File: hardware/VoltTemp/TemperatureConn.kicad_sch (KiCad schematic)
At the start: 3 parts, among them J15 Conn_01x07, J6 Conn_01x04

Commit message: schematic mostly done
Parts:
- removed J15: Conn_01x07, symbol Connector_Generic:Conn_01x07
- added J8: Conn_01x06, VoltTemp:1053131106, symbol Connector_Generic:Conn_01x06
- added J9: Conn_01x03, VoltTemp:1053131103, symbol Connector_Generic:Conn_01x03
- J6: footprint (none) -> VoltTemp:1053132104; P/N (none) -> 1053132104
- R24: footprint Resistor_SMD:R_0805_2012Metric -> Resistor_SMD:R_0603_1608Metric_Pad0.98x0.95mm_HandSolder; P/N SMD_0805 -> (none)
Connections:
- net GNDA: now also J8.6 (Pin_6), J9.3 (Pin_3)
- net VDDA: now also J8.1 (Pin_1), J9.1 (Pin_1)
- net rawTemperature0: now also J6.2 (Pin_2), R24.1
- net rawTemperature1: now also J8.4 (Pin_4); no longer J6.2 (Pin_2), R24.1
- net rawTemperature2: now also J8.3 (Pin_3)
- net rawTemperature3: now also J8.2 (Pin_2)
- net rawTemperature4: now also J9.2 (Pin_2)
- net rawTemperature1_Pre renamed rawTemperature0_Pre
- net rawTemperature0_Pre: now also J8.5 (Pin_5)
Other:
- note added: "Extra Temperature Breakout"
- note added: "Thermistor Collector Connector"

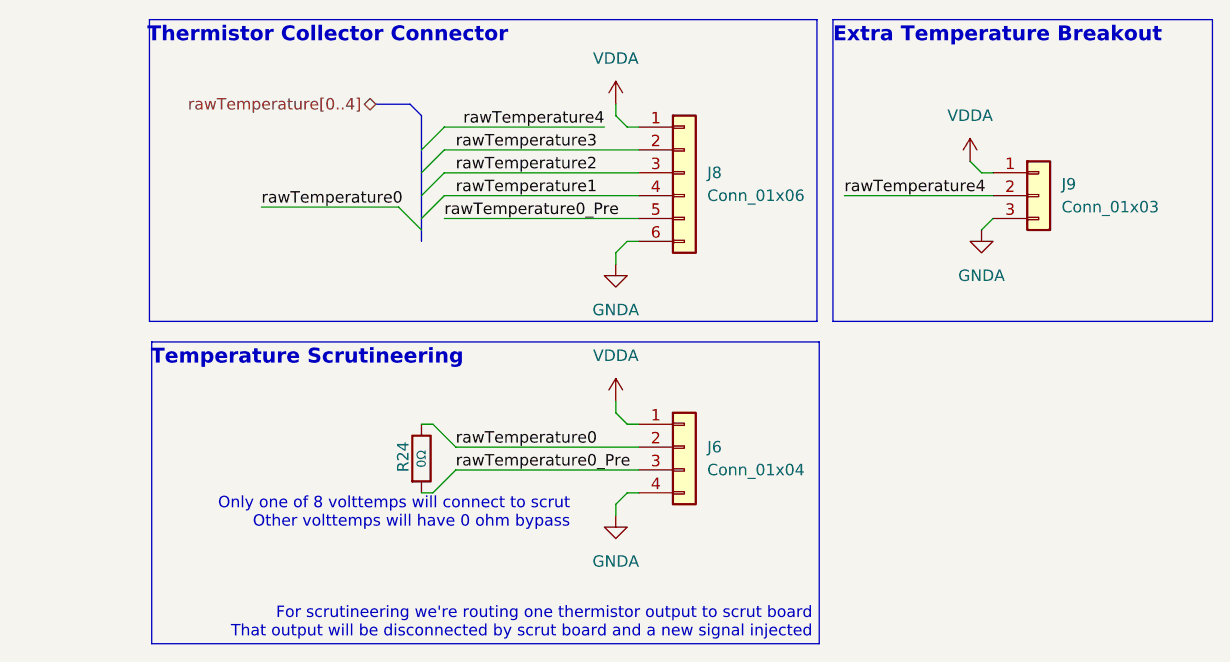
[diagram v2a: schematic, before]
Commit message: add thermistor test board, just need to route volttemp testpoints
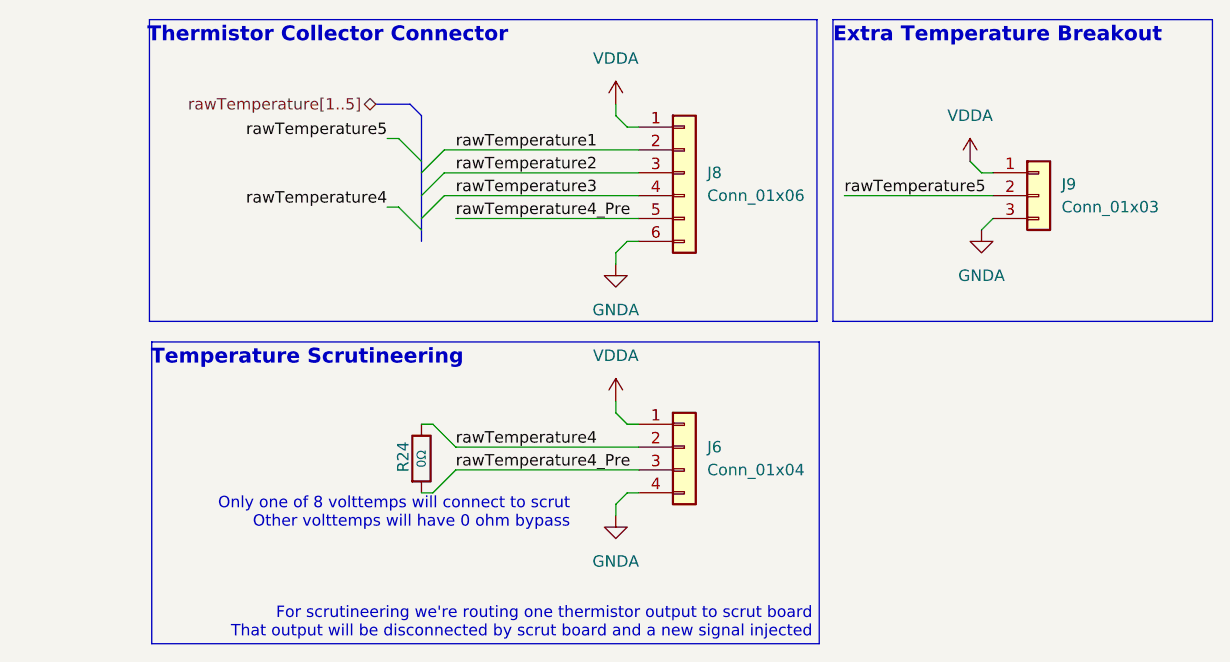
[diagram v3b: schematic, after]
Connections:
- net rawTemperature0 is gone; now on net rawTemperature4: J6.2 (Pin_2), R24.1
- net rawTemperature1: now also J8.2 (Pin_2); no longer J8.4 (Pin_4)
- net rawTemperature3: now also J8.4 (Pin_4); no longer J8.2 (Pin_2)
- net rawTemperature4: no longer J9.2 (Pin_2)
- net rawTemperature0_Pre renamed rawTemperature4_Pre
- new net rawTemperature5: J9.2 (Pin_2)
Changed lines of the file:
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@@
+	)
+	(bus_entry
+		(at 60.96 62.23)
+		(size 2.54 2.54)
+		(stroke
+			(width 0)
+			(type default)
+		)
+	)
+	(bus_entry
+		(at 63.5 71.12)
+		(size 2.54 -2.54)
+		(stroke
+			(width 0)
+			(type default)
+		)
 	)
 	(bus_entry
@@
 		)
 	)
-	(bus_entry
-		(at 63.5 71.12)
-		(size 2.54 -2.54)
-		(stroke
-			(width 0)
-			(type default)
-		)
-	)
-	(bus_entry
-		(at 63.5 63.5)
-		(size 2.54 -2.54)
-		(stroke
-			(width 0)
-			(type default)
-		)
-	)
 	(wire
 		(pts
@@
 	(wire
 		(pts
+			(xy 59.69 62.23) (xy 60.96 62.23)
+		)
+		(stroke
+			(width 0)
+			(type default)
+		)
+	)
+	(wire
+		(pts
 			(xy 86.36 93.98) (xy 85.09 92.71)
 		)
@@
 	(bus
 		(pts
-			(xy 63.5 68.58) (xy 63.5 66.04)
-		)
-		(stroke
-			(width 0)
-			(type default)
-		)
-	)
-	(wire
-		(pts
-			(xy 45.72 69.85) (xy 60.96 69.85)
-		)
-		(stroke
-			(width 0)
-			(type default)
-		)
-	)
-	(bus
-		(pts
-			(xy 63.5 63.5) (xy 63.5 59.69)
+			(xy 63.5 66.04) (xy 63.5 68.58)
+		)
+		(stroke
+			(width 0)
+			(type default)
+		)
+	)
+	(bus
+		(pts
+			(xy 63.5 66.04) (xy 63.5 64.77)
 		)
 		(stroke
@@
 	(wire
 		(pts
+			(xy 85.09 91.44) (xy 85.09 92.71)
+		)
+		(stroke
+			(width 0)
+			(type default)
+		)
+	)
+	(wire
+		(pts
+			(xy 67.31 99.06) (xy 87.63 99.06)
+		)
+		(stroke
+			(width 0)
+			(type default)
+		)
+	)
+	(wire
+		(pts
+			(xy 63.5 93.98) (xy 64.77 93.98)
+		)
+		(stroke
+			(width 0)
+			(type default)
+		)
+	)
+	(wire
+		(pts
+			(xy 110.49 68.58) (xy 127 68.58)
+		)
+		(stroke
+			(width 0)
+			(type default)
+		)
+	)
+	(bus
+		(pts
+			(xy 63.5 59.69) (xy 62.23 58.42)
+		)
+		(stroke
+			(width 0)
+			(type default)
+		)
+	)
+	(wire
+		(pts
+			(xy 67.31 96.52) (xy 87.63 96.52)
+		)
+		(stroke
+			(width 0)
+			(type default)
+		)
+	)
+	(wire
+		(pts
+			(xy 59.69 69.85) (xy 60.96 69.85)
+		)
+		(stroke
+			(width 0)
+			(type default)
+		)
+	)
+	(bus
+		(pts
+			(xy 58.42 58.42) (xy 62.23 58.42)
+		)
+		(stroke
+			(width 0)
+			(type default)
+		)
+	)
+	(bus
+		(pts
+			(xy 63.5 64.77) (xy 63.5 59.69)
+		)
+		(stroke
+			(width 0)
+			(type default)
+		)
+	)
+	(bus
+		(pts
+			(xy 63.5 71.12) (xy 63.5 72.39)
+		)
+		(stroke
+			(width 0)
+			(type default)
+		)
+	)
+	(wire
+		(pts
+			(xy 64.77 93.98) (xy 67.31 96.52)
+		)
+		(stroke
+			(width 0)
+			(type default)
+		)
+	)
+	(wire
+		(pts
+			(xy 66.04 63.5) (xy 87.63 63.5)
+		)
+		(stroke
+			(width 0)
+			(type default)
+		)
+	)
+	(wire
+		(pts
 			(xy 66.04 68.58) (xy 87.63 68.58)
 		)
@@
 	(wire
 		(pts
-			(xy 66.04 71.12) (xy 87.63 71.12)
-		)
-		(stroke
-			(width 0)
-			(type default)
-		)
-	)
-	(bus
-		(pts
-			(xy 63.5 71.12) (xy 63.5 72.39)
-		)
-		(stroke
-			(width 0)
-			(type default)
-		)
-	)
-	(wire
-		(pts
-			(xy 85.09 91.44) (xy 85.09 92.71)
-		)
-		(stroke
-			(width 0)
-			(type default)
-		)
-	)
-	(wire
-		(pts
-			(xy 67.31 99.06) (xy 87.63 99.06)
-		)
-		(stroke
-			(width 0)
-			(type default)
-		)
-	)
-	(wire
-		(pts
-			(xy 63.5 93.98) (xy 64.77 93.98)
-		)
-		(stroke
-			(width 0)
-			(type default)
-		)
-	)
-	(wire
-		(pts
-			(xy 66.04 63.5) (xy 87.63 63.5)
-		)
-		(stroke
-			(width 0)
-			(type default)
-		)
-	)
-	(wire
-		(pts
-			(xy 110.49 68.58) (xy 127 68.58)
-		)
-		(stroke
-			(width 0)
-			(type default)
-		)
-	)
-	(bus
-		(pts
-			(xy 63.5 59.69) (xy 62.23 58.42)
-		)
-		(stroke
-			(width 0)
-			(type default)
-		)
-	)
-	(wire
-		(pts
-			(xy 67.31 96.52) (xy 87.63 96.52)
-		)
-		(stroke
-			(width 0)
-			(type default)
-		)
-	)
-	(bus
-		(pts
-			(xy 58.42 58.42) (xy 62.23 58.42)
+			(xy 66.04 66.04) (xy 87.63 66.04)
 		)
 		(stroke
@@
 	(wire
 		(pts
-			(xy 64.77 93.98) (xy 67.31 96.52)
-		)
-		(stroke
-			(width 0)
-			(type default)
-		)
-	)
-	(wire
-		(pts
-			(xy 66.04 66.04) (xy 87.63 66.04)
-		)
-		(stroke
-			(width 0)
-			(type default)
-		)
-	)
-	(wire
-		(pts
 			(xy 85.09 76.2) (xy 85.09 74.93)
 		)
@@
 	(wire
 		(pts
-			(xy 66.04 60.96) (xy 83.82 60.96)
-		)
-		(stroke
-			(width 0)
-			(type default)
-		)
-	)
-	(wire
-		(pts
 			(xy 86.36 101.6) (xy 87.63 101.6)
 		)
@@
 		)
 	)
-	(bus
-		(pts
-			(xy 63.5 66.04) (xy 63.5 63.5)
-		)
-		(stroke
-			(width 0)
-			(type default)
-		)
-	)
 	(wire
 		(pts
@@
 		)
 	)
-	(label "rawTemperature0"
-		(at 45.72 69.85 0)
-		(effects
-			(font
-				(size 1.27 1.27)
-			)
-			(justify left bottom)
-		)
-	)
-	(label "rawTemperature0"
+	(wire
+		(pts
+			(xy 67.31 71.12) (xy 87.63 71.12)
+		)
+		(stroke
+			(width 0)
+			(type default)
+		)
+	)
+	(label "rawTemperature4"
 		(at 67.31 96.52 0)
 		(effects
@@
 		)
 	)
-	(label "rawTemperature0_Pre"
+	(label "rawTemperature4_Pre"
 		(at 67.31 99.06 0)
 		(effects
@@
 		)
 	)
+	(label "rawTemperature4_Pre"
+		(at 67.31 71.12 0)
+		(effects
+			(font
+				(size 1.27 1.27)
+			)
+			(justify left bottom)
+		)
+	)
 	(label "rawTemperature3"
-		(at 67.31 63.5 0)
-		(effects
-			(font
-				(size 1.27 1.27)
-			)
-			(justify left bottom)
+		(at 67.31 68.58 0)
+		(effects
+			(font
+				(size 1.27 1.27)
+			)
+			(justify left bottom)
+		)
+	)
+	(label "rawTemperature4"
+		(at 59.69 69.85 180)
+		(effects
+			(font
+				(size 1.27 1.27)
+			)
+			(justify right bottom)
+		)
+	)
+	(label "rawTemperature5"
+		(at 59.69 62.23 180)
+		(effects
+			(font
+				(size 1.27 1.27)
+			)
+			(justify right bottom)
 		)
 	)
@@
 		)
 	)
-	(label "rawTemperature4"
-		(at 83.82 60.96 180)
-		(effects
-			(font
-				(size 1.27 1.27)
-			)
-			(justify right bottom)
+	(label "rawTemperature5"
+		(at 110.49 68.58 0)
+		(effects
+			(font
+				(size 1.27 1.27)
+			)
+			(justify left bottom)
 		)
 	)
 	(label "rawTemperature1"
-		(at 67.31 68.58 0)
-		(effects
-			(font
-				(size 1.27 1.27)
-			)
-			(justify left bottom)
-		)
-	)
-	(label "rawTemperature4"
-		(at 110.49 68.58 0)
-		(effects
-			(font
-				(size 1.27 1.27)
-			)
-			(justify left bottom)
-		)
-	)
-	(label "rawTemperature0_Pre"
-		(at 66.04 71.12 0)
-		(effects
-			(font
-				(size 1.27 1.27)
-			)
-			(justify left bottom)
-		)
-	)
-	(hierarchical_label "rawTemperature[0..4]"
+		(at 67.31 63.5 0)
+		(effects
+			(font
+				(size 1.27 1.27)
+			)
+			(justify left bottom)
+		)
+	)
+	(hierarchical_label "rawTemperature[1..5]"
 		(shape bidirectional)
 		(at 58.42 58.42 180)

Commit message: Bom (#3)
* bom

* bom for cell sim and thermistor

* stopped displaying part numbers in schematic
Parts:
- R24: P/N (none) -> SFR03EZPJ000
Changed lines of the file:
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@@
+			)
+		)
+		(property "Id" ""
+			(at 92.71 66.04 0)
+			(effects
+				(font
+					(size 1.27 1.27)
+				)
+			)
+		)
+		(property "MANUFACTURER" ""
+			(at 92.71 66.04 0)
+			(effects
+				(font
+					(size 1.27 1.27)
+				)
+			)
+		)
+		(property "MAXIMUM_PACKAGE_HEIGHT" ""
+			(at 92.71 66.04 0)
+			(effects
+				(font
+					(size 1.27 1.27)
+				)
+			)
+		)
+		(property "PARTREV" ""
+			(at 92.71 66.04 0)
+			(effects
+				(font
+					(size 1.27 1.27)
+				)
+			)
+		)
+		(property "STANDARD" ""
+			(at 92.71 66.04 0)
+			(effects
+				(font
+					(size 1.27 1.27)
+				)
+			)
+		)
+		(property "Vds" ""
+			(at 92.71 66.04 0)
+			(effects
+				(font
+					(size 1.27 1.27)
+				)
 			)
 		)
@@
 			)
 		)
+		(property "Id" ""
+			(at 92.71 96.52 0)
+			(effects
+				(font
+					(size 1.27 1.27)
+				)
+			)
+		)
+		(property "MANUFACTURER" ""
+			(at 92.71 96.52 0)
+			(effects
+				(font
+					(size 1.27 1.27)
+				)
+			)
+		)
+		(property "MAXIMUM_PACKAGE_HEIGHT" ""
+			(at 92.71 96.52 0)
+			(effects
+				(font
+					(size 1.27 1.27)
+				)
+			)
+		)
+		(property "PARTREV" ""
+			(at 92.71 96.52 0)
+			(effects
+				(font
+					(size 1.27 1.27)
+				)
+			)
+		)
+		(property "STANDARD" ""
+			(at 92.71 96.52 0)
+			(effects
+				(font
+					(size 1.27 1.27)
+				)
+			)
+		)
+		(property "Vds" ""
+			(at 92.71 96.52 0)
+			(effects
+				(font
+					(size 1.27 1.27)
+				)
+			)
+		)
 		(pin "1"
 		)
@@
 			)
 		)
-		(property "Datasheet" "~"
+		(property "Datasheet" "https://www.mouser.com/ProductDetail/Panasonic/ERA-3AED822V?qs=yocZuyCaXdPY%252BoKbtgBWEA%3D%3D&srsltid=AfmBOoqNGSzjo0BSOm8a05aF1OD2DC1DEesdZm6KpS4h-eMhVajjmgo9"
 			(at 63.5 97.79 0)
 			(effects
@@
 			)
 		)
-		(property "P/N" ""
-			(at 63.5 97.79 0)
-			(effects
-				(font
-					(size 1.27 1.27)
-				)
-				(hide yes)
+		(property "P/N" "SFR03EZPJ000"
+			(at 63.5 97.79 0)
+			(effects
+				(font
+					(size 1.27 1.27)
+				)
+				(hide yes)
+			)
+		)
+		(property "Id" ""
+			(at 63.5 97.79 0)
+			(effects
+				(font
+					(size 1.27 1.27)
+				)
+			)
+		)
+		(property "MANUFACTURER" ""
+			(at 63.5 97.79 0)
+			(effects
+				(font
+					(size 1.27 1.27)
+				)
+			)
+		)
+		(property "MAXIMUM_PACKAGE_HEIGHT" ""
+			(at 63.5 97.79 0)
+			(effects
+				(font
+					(size 1.27 1.27)
+				)
+			)
+		)
+		(property "PARTREV" ""
+			(at 63.5 97.79 0)
+			(effects
+				(font
+					(size 1.27 1.27)
+				)
+			)
+		)
+		(property "STANDARD" ""
+			(at 63.5 97.79 0)
+			(effects
+				(font
+					(size 1.27 1.27)
+				)
+			)
+		)
+		(property "Vds" ""
+			(at 63.5 97.79 0)
+			(effects
+				(font
+					(size 1.27 1.27)
+				)
 			)
 		)
@@
 			)
 		)
+		(property "Id" ""
+			(at 132.08 68.58 0)
+			(effects
+				(font
+					(size 1.27 1.27)
+				)
+			)
+		)
+		(property "MANUFACTURER" ""
+			(at 132.08 68.58 0)
+			(effects
+				(font
+					(size 1.27 1.27)
+				)
+			)
+		)
+		(property "MAXIMUM_PACKAGE_HEIGHT" ""
+			(at 132.08 68.58 0)
+			(effects
+				(font
+					(size 1.27 1.27)
+				)
+			)
+		)
+		(property "PARTREV" ""
+			(at 132.08 68.58 0)
+			(effects
+				(font
+					(size 1.27 1.27)
+				)
+			)
+		)
+		(property "STANDARD" ""
+			(at 132.08 68.58 0)
+			(effects
+				(font
+					(size 1.27 1.27)
+				)
+			)
+		)
+		(property "Vds" ""
+			(at 132.08 68.58 0)
+			(effects
+				(font
+					(size 1.27 1.27)
+				)
+			)
+		)

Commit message: this is the staircase board :(
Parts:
- removed J6: Conn_01x04, VoltTemp:1053132104, symbol Connector_Generic:Conn_01x04
- removed R24: 0Ω, Resistor_SMD:R_0603_1608Metric_Pad0.98x0.95mm_HandSolder, symbol Device:R
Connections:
- net rawTemperature4_Pre renamed rawTemp4_PRE
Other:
- note removed: "For scrutineering we're routing one thermistor output to scrut board That output will be disconnected by scrut board and a new signal injected"
- note removed: "Only one of 8 volttemps will connect to scrut Other volttemps will have 0 ohm bypass"
- note removed: "Temperature Scrutineering"
